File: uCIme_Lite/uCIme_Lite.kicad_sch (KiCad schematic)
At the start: 15 parts, among them J2 JACK_POWER_IN, J3 USB_POWER_IN, J4 USB_PC, J5 GPIO, J6 5V_ENABLE, J7 SERIAL, J8 JACK_POWER_OUT, J9 USB_POWER_OUT

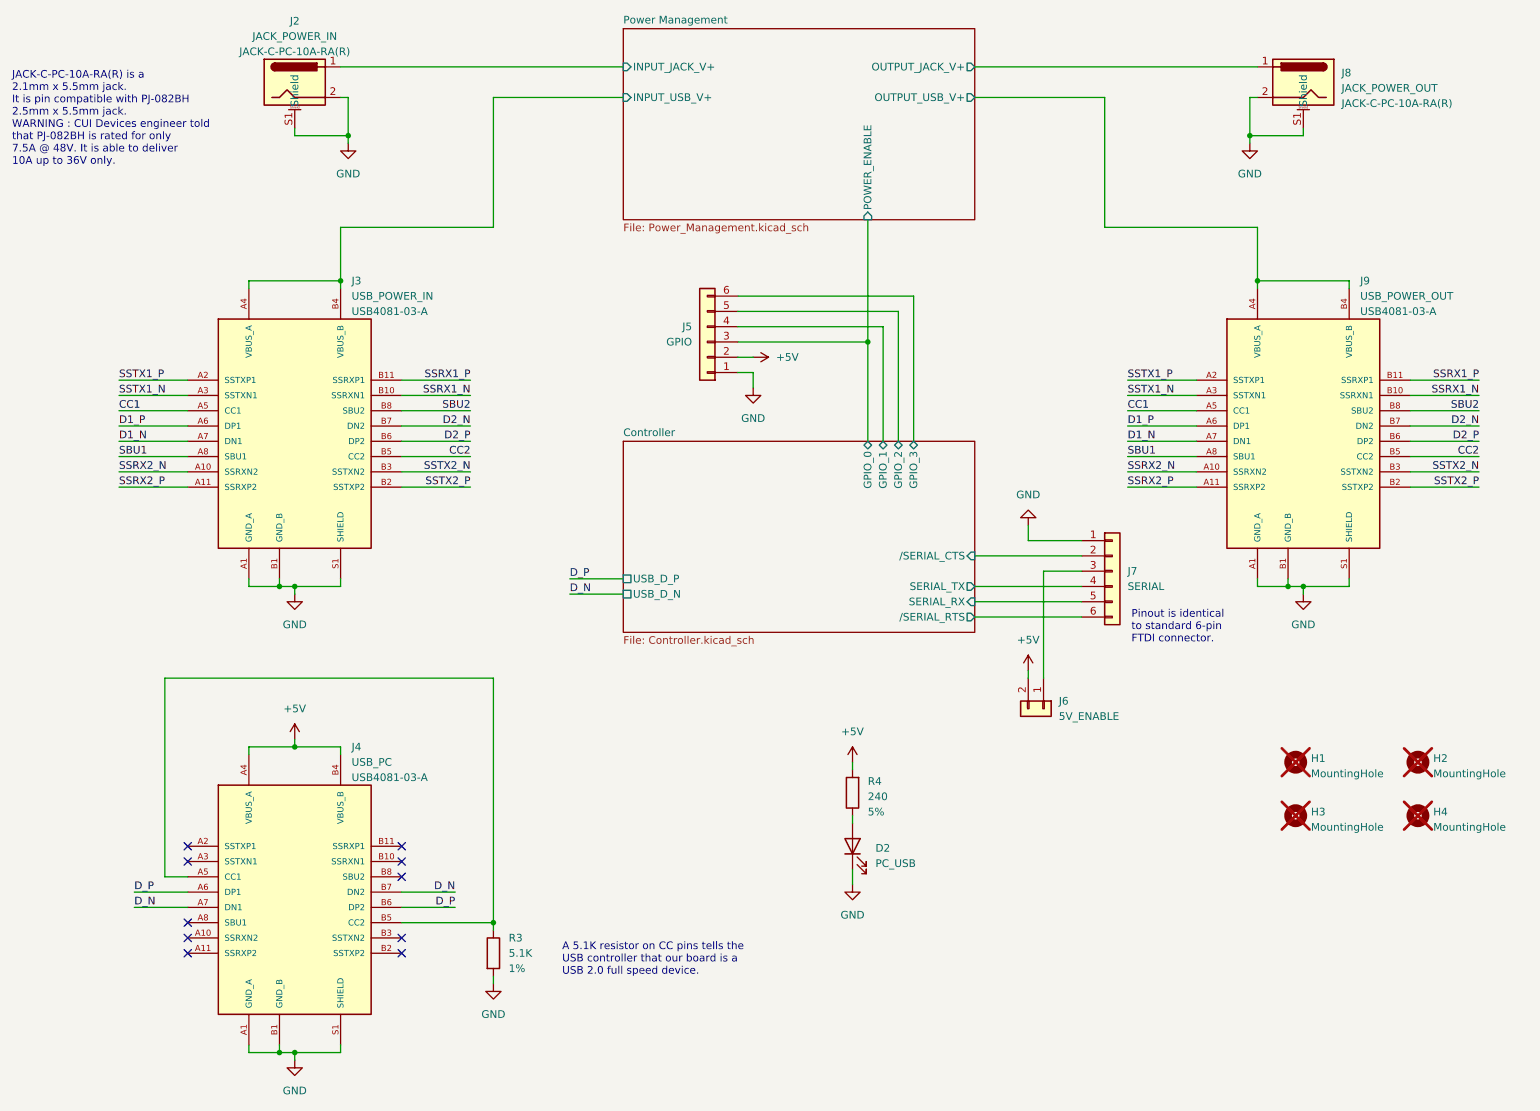
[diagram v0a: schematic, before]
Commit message: lite: Merged serial and GPIO single-row pin headers in a double-row pin header to save some space on the PCB, only the schematic is currently updated.
Signed-off-by: Adrien Ricciardi <aricciardi@baylibre.com>
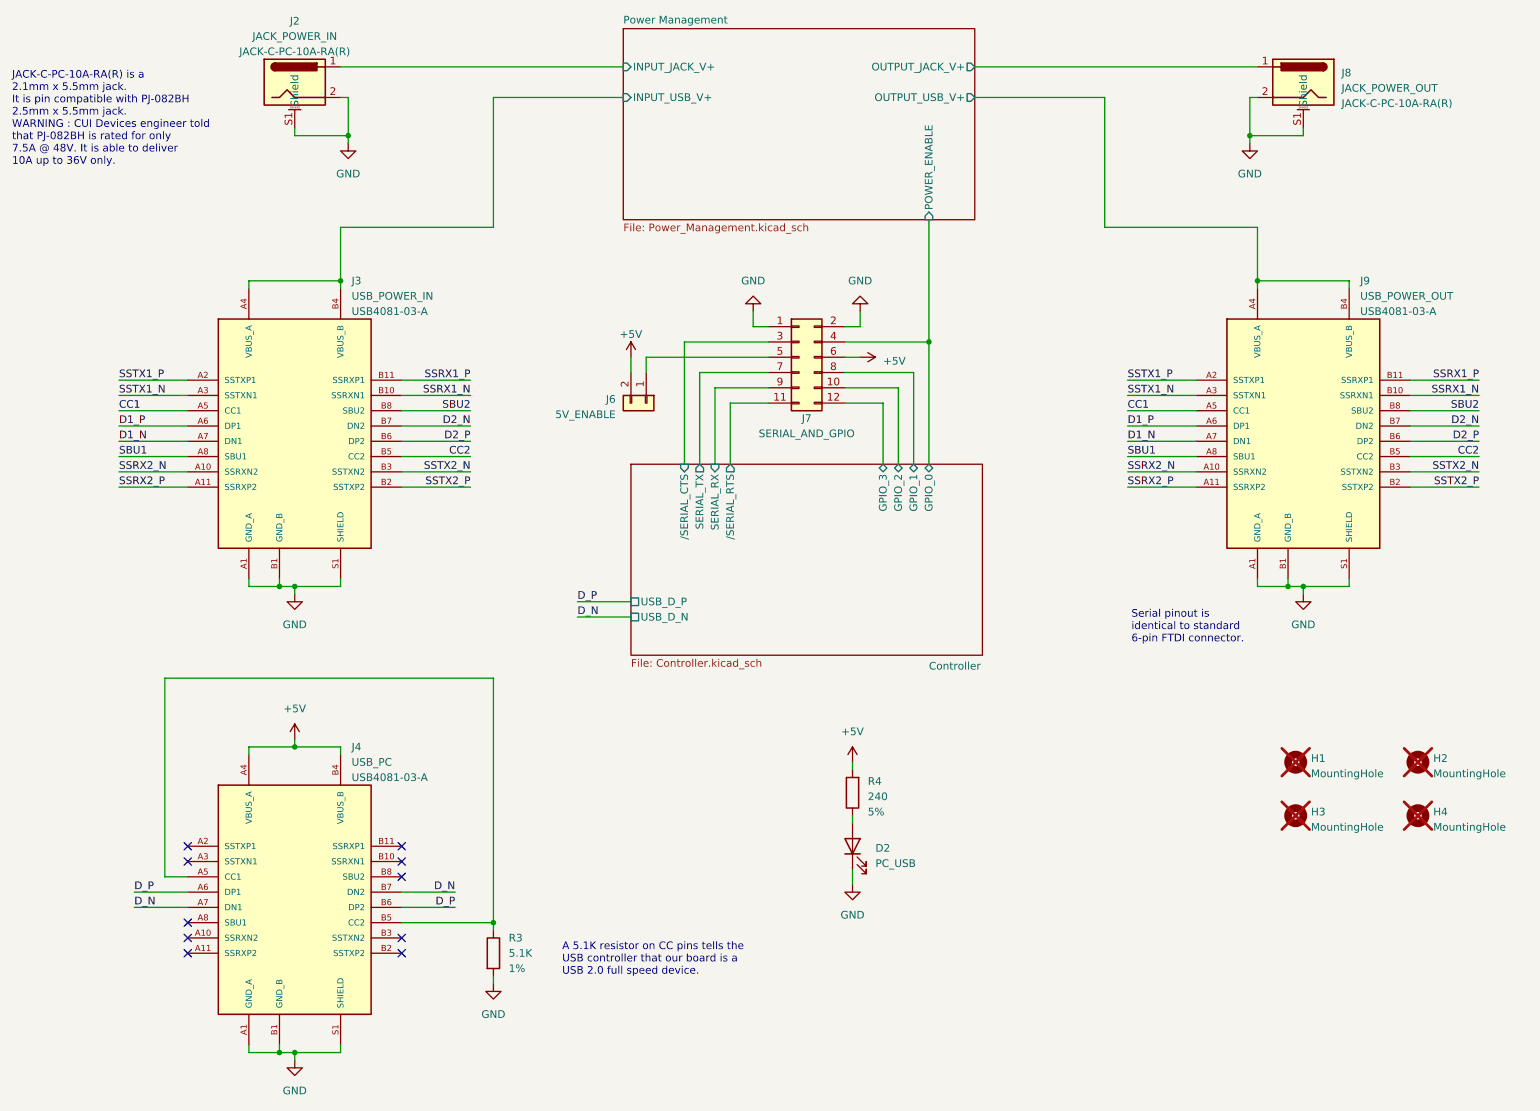
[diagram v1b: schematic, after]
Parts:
- removed J5: GPIO, Connector_PinHeader_2.54mm:PinHeader_1x06_P2.54mm_Horizontal, symbol Connector_Generic:Conn_01x06
- J7: value SERIAL -> SERIAL_AND_GPIO; footprint Connector_PinHeader_2.54mm:PinHeader_1x06_P2.54mm_Horizontal -> Connector_PinHeader_2.54mm:PinHeader_2x06_P2.54mm_Horizontal; symbol Connector_Generic:Conn_01x06 -> Connector_Generic:Conn_02x06_Odd_Even
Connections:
- net +5V: now also J7.6 (Pin_6)
- net Controller/GPIO_0: now also J7.4 (Pin_4)
- net Controller/GPIO_1: now also J7.8 (Pin_8)
- net Controller/GPIO_2: now also J7.10 (Pin_10)
- net Controller/GPIO_3: now also J7.12 (Pin_12)
- net Controller/SERIAL_RX: now also J7.9 (Pin_9); no longer J7.5 (Pin_5)
- net Controller/SERIAL_TX: now also J7.7 (Pin_7); no longer J7.4 (Pin_4)
- net Controller//SERIAL_CTS: now also J7.3 (Pin_3); no longer J7.2 (Pin_2)
- net Controller//SERIAL_RTS: now also J7.11 (Pin_11); no longer J7.6 (Pin_6)
- net GND: now also J7.2 (Pin_2)
- net at J6.1 (Pin_1): now also J7.5 (Pin_5); no longer J7.3 (Pin_3)
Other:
- note added: "Serial pinout is identical to standard 6-pin FTDI connector."
- note removed: "Pinout is identical to standard 6-pin FTDI connector."
- moved on the sheet: J6

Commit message: lite: Added Aisler part number properties in both schematic and PCB.
Signed-off-by: Adrien Ricciardi <aricciardi@baylibre.com>
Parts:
- D2: AISLER_MPN (none) -> 150080SS75000
- J2, J8: AISLER_MPN (none) -> JACK-C-PC-10A-RA(R)
- J3, J4, J9: AISLER_MPN (none) -> USB4081-03-A
- R3: AISLER_MPN (none) -> 5.1K 1% 0603
- R4: AISLER_MPN (none) -> 240 5% 1206
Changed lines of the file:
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@@
+      (effects (font (size 1.27 1.27)) hide)
+    )
+    (property "AISLER_MPN" "150080SS75000" (at 154.94 153.67 0)
       (effects (font (size 1.27 1.27)) hide)
     )
@@
     (property "PartNumber" "JACK-C-PC-10A-RA(R)" (at 236.22 30.2006 0)
       (effects (font (size 1.27 1.27)) (justify right))
+    )
+    (property "AISLER_MPN" "JACK-C-PC-10A-RA(R)" (at 229.87 26.67 0)
+      (effects (font (size 1.27 1.27)) hide)
     )
     (pin "1")
@@
       (effects (font (size 1.27 1.27)) hide)
     )
+    (property "AISLER_MPN" "5.1K 1% 0603" (at 95.25 171.45 0)
+      (effects (font (size 1.27 1.27)) hide)
+    )
     (pin "1")
     (pin "2")
@@
     (property "PartNumber" "JACK-C-PC-10A-RA(R)" (at 62.23 21.59 0)
       (effects (font (size 1.27 1.27)))
+    )
+    (property "AISLER_MPN" "JACK-C-PC-10A-RA(R)" (at 62.23 26.67 0)
+      (effects (font (size 1.27 1.27)) hide)
     )
     (pin "1")
@@
     (property "PartNumber" "USB4081-03-A" (at 71.6789 64.77 0)
       (effects (font (size 1.27 1.27)) (justify left))
+    )
+    (property "AISLER_MPN" "USB4081-03-A" (at 62.23 86.36 0)
+      (effects (font (size 1.27 1.27)) hide)
     )
     (pin "A1")
@@
       (effects (font (size 1.27 1.27)) (justify right))
     )
+    (property "AISLER_MPN" "240 5% 1206" (at 154.94 144.78 0)
+      (effects (font (size 1.27 1.27)) hide)
+    )
     (pin "1")
     (pin "2")
@@
     (property "PartNumber" "USB4081-03-A" (at 71.6789 142.24 0)
       (effects (font (size 1.27 1.27)) (justify left))
+    )
+    (property "AISLER_MPN" "USB4081-03-A" (at 62.23 163.83 0)
+      (effects (font (size 1.27 1.27)) hide)
     )
     (pin "A1")
@@
       (effects (font (size 1.27 1.27)) (justify left))
     )
+    (property "AISLER_MPN" "USB4081-03-A" (at 229.87 86.36 0)
+      (effects (font (size 1.27 1.27)) hide)
+    )
     (pin "A1")
